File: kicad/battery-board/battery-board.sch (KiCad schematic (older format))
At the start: 38 parts, among them K1 CONN_3, K2 CONN_3, K3 CONN_3, K4 CONN_3, K5 CONN_3, K6 CONN_3, P1 CONN_5, SW1 SW_PUSH_SMALL, U1 PANSTAMP_02, U2 BMP085, U3 DHT22, U4 MAX1724, U5 TMP36

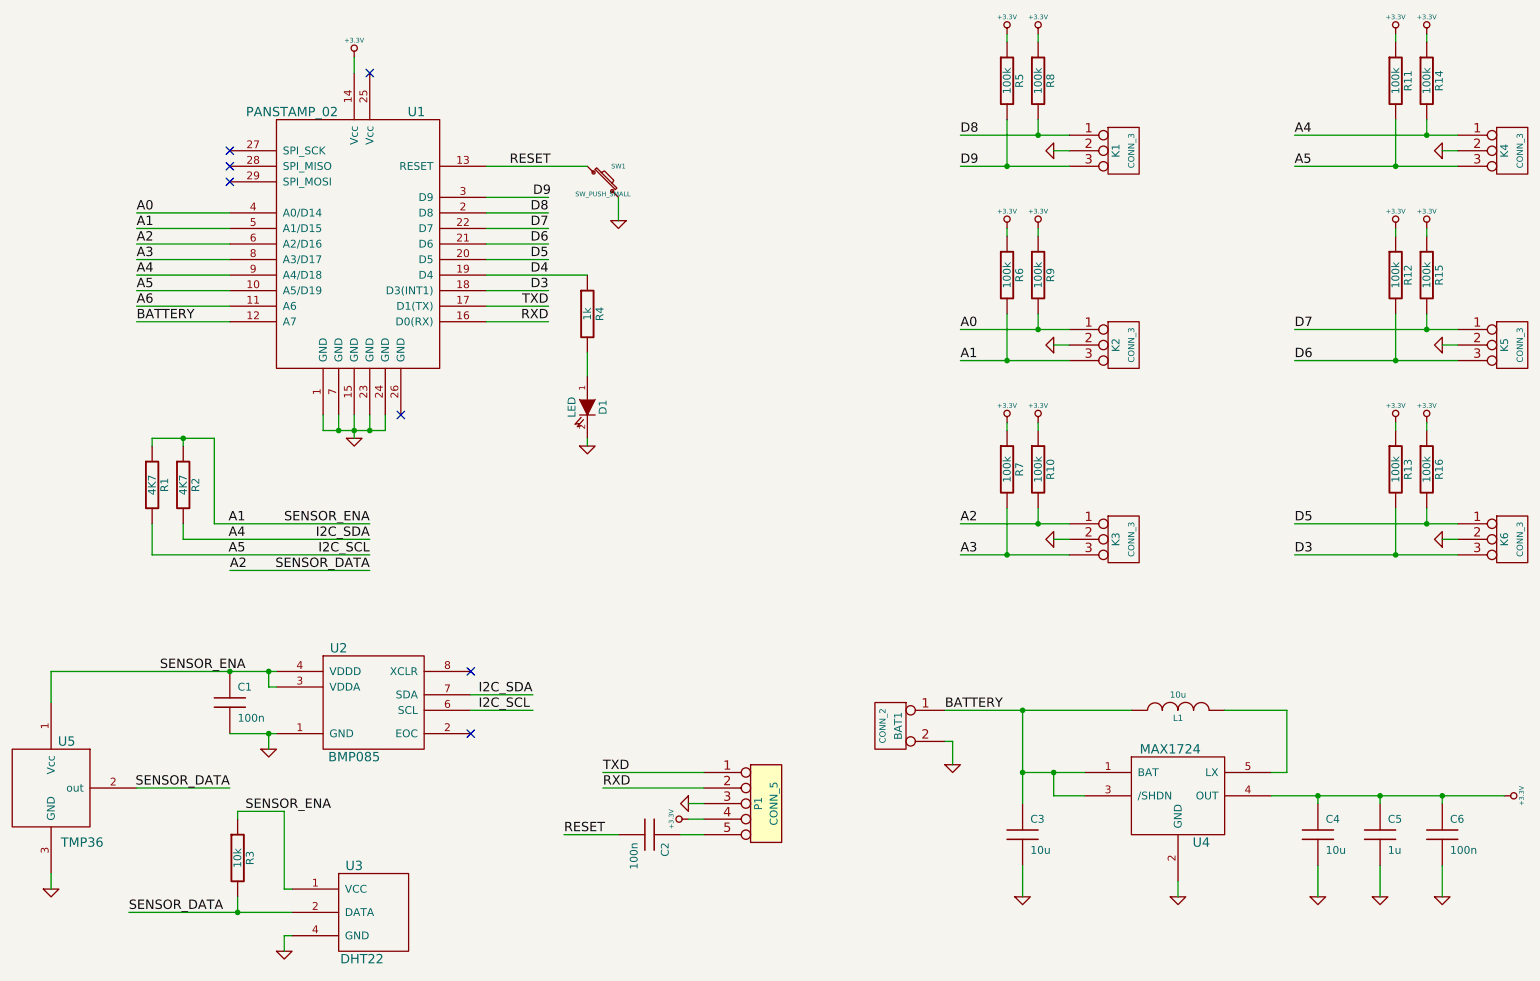
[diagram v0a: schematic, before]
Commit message: Added grove connector for the I2C lines
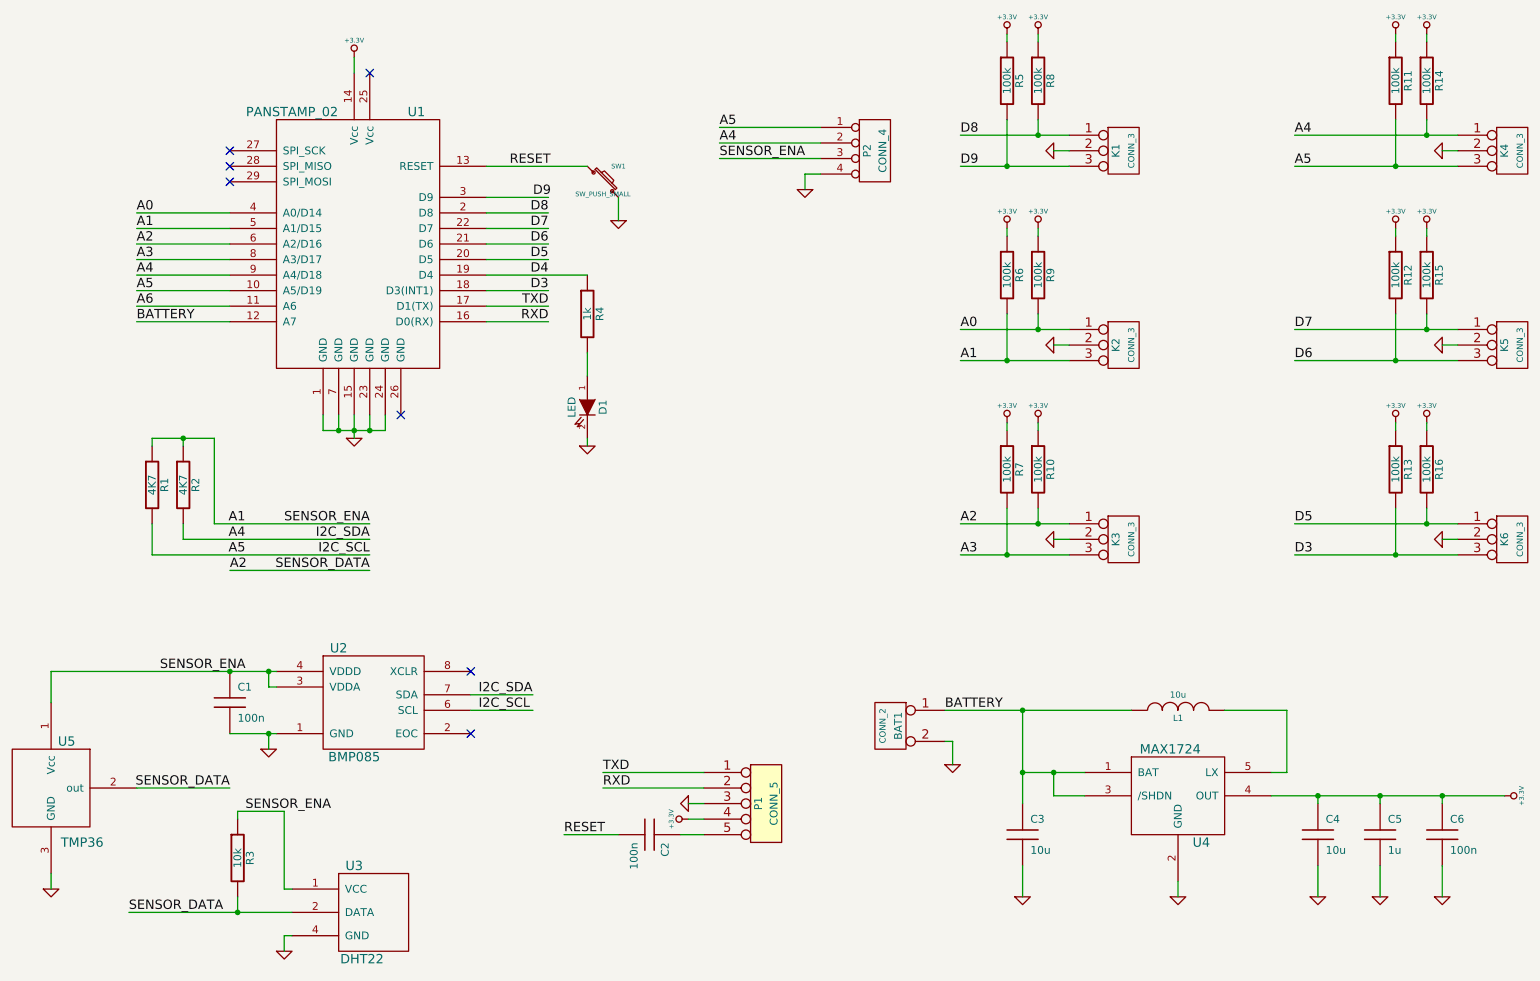
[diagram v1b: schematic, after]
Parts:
- added P2: CONN_4, GROVE_MALE, symbol CONN_4
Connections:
- net A1: now also P2.3 (P3)
- net A4: now also P2.2 (P2)
- net A5: now also P2.1 (P1)
- net GND: now also P2.4 (P4)
